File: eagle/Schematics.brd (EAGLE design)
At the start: 65 x 56 mm, 56 parts, among them K1 PIN20X2

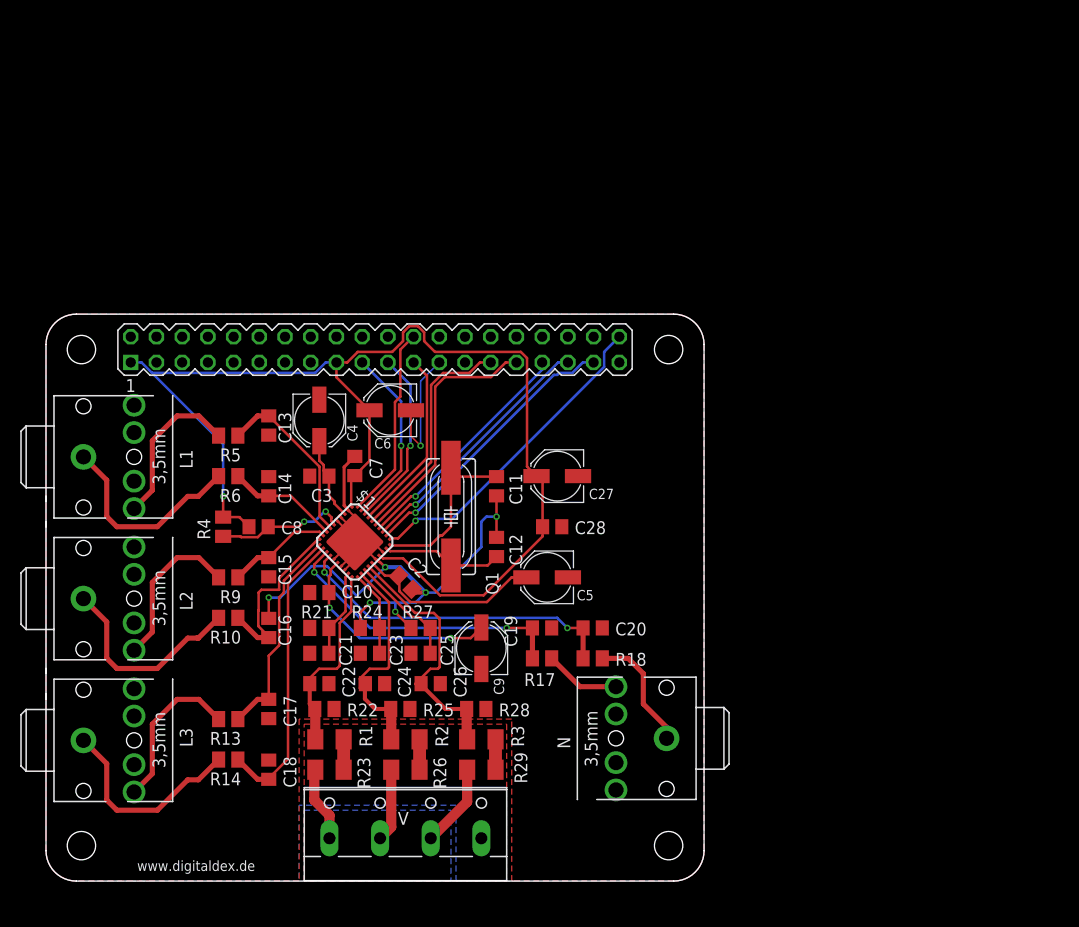
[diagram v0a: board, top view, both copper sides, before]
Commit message: fixed symbol; routed GND; rerouted some signals with more space
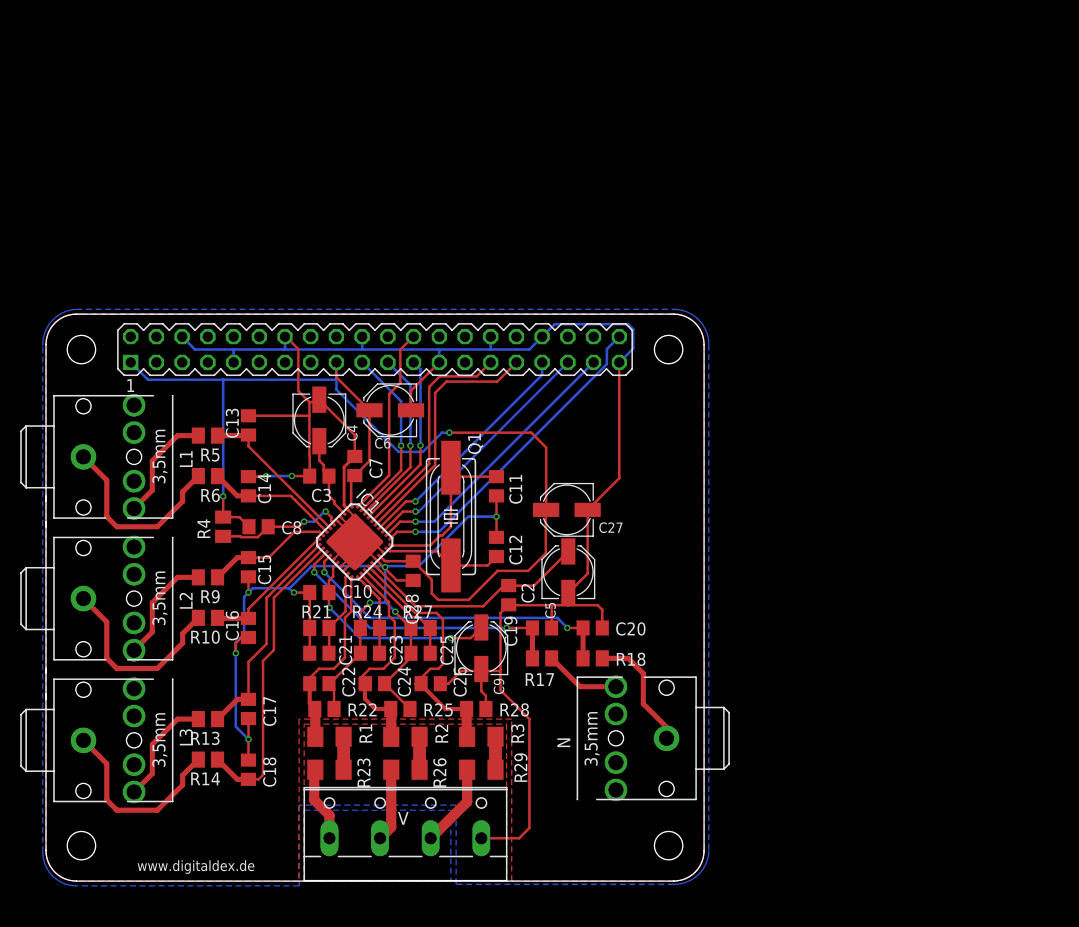
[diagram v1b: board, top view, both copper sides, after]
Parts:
- moved C28 14.4 mm to (36.3, 30.6), turned to 270 degrees
- moved C2 10.3 mm to (45.7, 28.2), turned to 270 degrees
- moved C27 3.47 mm to (51.5, 36.7)
- moved C5 2.15 mm to (51.6, 30.5), turned to 90 degrees
- moved C14 2.00 mm to (20.0, 39.0)
- moved C15 2.00 mm to (20.0, 31.0)
- moved C16 2.00 mm to (20.0, 25.0), turned to 270 degrees
- moved C17 2.00 mm to (20.0, 17.0)
- moved C18 2.00 mm to (20.0, 11.0)
- moved R10 2.00 mm to (16.0, 26.0)
- moved R13 2.00 mm to (16.0, 16.0)
- moved R14 2.00 mm to (16.0, 12.0)
- moved R5 2.00 mm to (16.0, 44.0)
- moved R6 2.00 mm to (16.0, 40.0)
- moved R9 2.00 mm to (16.0, 30.0)
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- renumbered $1 to IC1
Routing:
- net GND: track 96.0 -> 307.2 mm, vias 7 -> 10
- net N$10: track 15.8 -> 11.0 mm
- net N$14: track 15.8 -> 11.0 mm
- net N$12: track 15.8 -> 11.0 mm
- net N$4: track 18.6 -> 23.3 mm
- net +3V3: track 118.5 -> 114.2 mm, vias 1 -> 2
- net IBN: track 17.6 -> 13.9 mm
- net IBP: track 10.4 -> 12.4 mm
- net IAN: track 11.0 -> 13.0 mm
- net IAP: track 17.4 -> 15.5 mm
- net N$13: track 20.5 -> 18.9 mm
- net N$15: track 20.4 -> 18.9 mm
- net N$11: track 20.4 -> 18.9 mm
- net ICN: track 29.2 -> 30.2 mm
- net N$3: track 23.2 -> 24.2 mm
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
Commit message: Changes
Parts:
- removed C14, C15, C16, C17, C18, C19, C20, C21, C22, C23, C24, C25, C26: 22nF, resistor:C0805
- removed C27: 10uF, resistor:PANASONIC_C
- removed C28: 0.1uF, resistor:C0805
- removed IC1: ADE9000, ADE9000:LFCSP40
- removed K1: PIN20X2, FLYFISH:PIN_20X2
- removed R10, R13, R14, R17, R18, R21, R22, R24, R25, R27, R28, R5, R6, R9: 1k, resistor:M0805
- removed R23, R26, R29: 500k, resistor:M1206
- removed R4: 10k, resistor:M0805
- removed V: (no value), con-wago-500:W237-4
- added ADE9000: ADE9000, ADE9000:LFCSP40
- added ADUM4151: ADUM4151, ADUM4151:SOIC20R
- added ADUM6404: ADUM6404, ADUM6404:SOIC16R
- added C1: 1uF, resistor:C0805
- added C100, C110, C120, C200, C201, C202, C500, C501, C510, C511, C520, C521, C530, C531: 22nF, resistor:C0805
- added C101, C111, C121: 51pF, resistor:C0805
- added C30, C32, C40, C42, C50, C52: 0.1uF, resistor:C0805
- added C31, C33, C41, C43, C51, C53: 10uF, resistor:C0805
- added IRM05-5: (no value), meanwell_irm_v6:IRM_05/10
- added JP1: (no value), adafruit:2X20
- added L: (no value), con-wago-500:W237-4
- added R100, R101, R102, R103, R110, R111, R112, R113, R120, R121, R122, R123: 200k, resistor:M1206
- added R104, R114, R124, R200, R201, R202, R500, R501, R510, R511, R520, R521, R530, R531: 1k, resistor:M0805
- added U$1, U$2, U$3, U$4: (no value), holes:2,8
- added U$5: ADP122AUJZ-3.3-R7, ADP122AUJZ-3.3-R7:TSOT23-5L
- C11: value 20pF -> 10uF
- C12: value 20pF -> 0.1uF
- C13: value 22nF -> 4.7uF
- C2: value 0.22uF -> 0.1uF
- C3: value 0.22uF -> 4.7uF
- C4: value 4.7uF -> 0.1uF; device resistor:PANASONIC_C -> resistor:C0805
- C5: device resistor:PANASONIC_C -> resistor:C0805
- C6: value 10uF -> 0.1uF; device resistor:PANASONIC_C -> resistor:C0805
- C7: value 0.1uF -> 4.7uF
- C8: value 1uF -> 18pF
- C9: value 4.7uF -> 18pF; device resistor:PANASONIC_C -> resistor:C0805
- Q1: device crystal:HC49UP -> crystal:CTS406
- R1, R2, R3: value 500k -> 10k; device resistor:M1206 -> resistor:M0805
- moved L3 66.3 mm to (66.0, 1.00), turned to 90 degrees
- moved L2 54.2 mm to (48.0, 1.00), turned to 90 degrees
- moved L1 50.2 mm to (30.0, 1.00), turned to 90 degrees
- moved C11 29.1 mm to (19.0, 53.0), turned to 0 degrees
- moved C10 27.7 mm to (14.0, 53.0)
- moved C4 27.7 mm to (53.0, 36.0), turned to 0 degrees
- moved C13 25.8 mm to (41.0, 30.0)
- moved N 23.9 mm to (84.0, 1.00), turned to 90 degrees
- moved R1 21.7 mm to (39.0, 33.0), turned to 270 degrees
- moved C7 21.7 mm to (52.0, 44.0)
- moved C8 20.9 mm to (41.0, 41.0), turned to 180 degrees
- moved R2 20.1 mm to (48.0, 30.0), turned to 90 degrees
- moved C9 20.1 mm to (45.0, 43.0)
- moved C3 18.9 mm to (43.0, 30.0), turned to 270 degrees
- moved R3 18.1 mm to (52.0, 30.0), turned to 270 degrees
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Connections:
- removed net +3V3: C27.+, C28.1, C6.+, C7.1, C8.1, IC1.1, IC1.27, K1.1, K1.17, R4.2
- removed net N$2: IC1.33, K1.35
- removed net N$24: IC1.39, K1.19
- removed net N$25: IC1.38, K1.21
- removed net N$26: IC1.37, K1.23
- removed net N$27: IC1.40, K1.24
- removed net N$5: C3.1, C4.+, IC1.3
- removed net N$6: C8.2, IC1.6, R4.1
- removed net N$7: C10.1, C9.+, IC1.16
- removed net N$8: C11.1, IC1.30, Q1.2
- removed net N$9: C12.2, IC1.29, Q1.1
- new net +3V3_ADE: ADE9000.1, ADE9000.27, ADE9000.4, ADUM4151.20, C12.1, C13.1, C32.1, C33.1, C52.1, C53.1, R1.2, R3.2, U$5.5
- new net +3V3_ISO: ADUM4151.1, C30.1, C31.1, JP1.1, JP1.17
- new net +5V_ADE: ADUM6404.10, ADUM6404.16, C42.1, C43.1, C50.1, C51.1, U$5.1, U$5.3
- new net +5V_ISO: ADUM6404.1, ADUM6404.7, C10.1, C11.1, C40.1, C41.1, IRM05-5.V+, JP1.2, JP1.4
- new net AGND: ADUM4151.10, ADUM4151.2, ADUM4151.9, ADUM6404.2, ADUM6404.8, C10.2, C11.2, C30.2, C31.2, C40.2, C41.2, IRM05-5.V-, JP1.14, JP1.20, JP1.25, JP1.30, JP1.34, JP1.39, JP1.6, JP1.9
- new net AVDDOUT: ADE9000.25, C6.1, C7.1
- new net CF1_ADE: ADE9000.33, ADUM6404.12
- new net CF1_ISO: ADUM6404.5, JP1.31
- new net CF2_ADE: ADE9000.34, ADUM6404.11
- new net CF2_ISO: ADUM6404.6, JP1.33
- new net CLKIN: ADE9000.29, C9.1, Q1.3
- new net CLKOUT: ADE9000.30, C8.1, Q1.1
- new net DVDDOUT: ADE9000.3, C2.1, C3.1
- new net IRQ0_ADE: ADE9000.31, ADUM6404.14
- new net IRQ0_ISO: ADUM6404.3, JP1.27
- new net IRQ1_ADE: ADE9000.32, ADUM6404.13
- new net IRQ1_ISO: ADUM6404.4, JP1.29
- new net MISO_ADE: ADE9000.38, ADUM4151.16
- new net MISO_ISO: ADUM4151.5, JP1.21
- new net MOSI_ADE: ADE9000.39, ADUM4151.17
- new net MOSI_ISO: ADUM4151.4, JP1.19
- new net PM1_ADE: ADE9000.5, ADUM4151.14, R2.2
- new net PM1_ISO: ADUM4151.7, JP1.35
- new net REF: ADE9000.16, C4.1, C5.1
- new net RESET_ADE: ADE9000.6, ADUM4151.13, C1.1, R3.1
- new net RESET_ISO: ADUM4151.8, JP1.37
- new net SCLK_ADE: ADE9000.37, ADUM4151.18
- new net SCLK_ISO: ADUM4151.3, JP1.23
- new net SS_ADE: ADE9000.40, ADUM4151.15, R1.1
- new net SS_ISO: ADUM4151.6, JP1.24
- net GND: now also ADE9000.15, ADE9000.17, ADE9000.18, ADE9000.2, ADE9000.26, ADE9000.28, ADE9000.35, ADE9000.36, ADE9000.GND, ADUM4151.11, ADUM4151.12, ADUM4151.19, ADUM6404.15, ADUM6404.9, C1.2, C100.1, C110.1, C12.2, C120.1, C13.2, C200.1, C201.1, C202.1, C32.2, C33.2, C4.2, C42.2, C43.2, C5.2, C50.2, C500.1, C501.2, C51.2, C510.1, C511.2, C52.2, C520.1, C521.2, C53.2, C530.1, C531.2, C6.2, C8.2, C9.2, IRM05-5.AC/N, L.4, R104.2, R114.2, R124.2, R2.1, R200.2, R201.2, R202.2, U$5.2, U$5.4; no longer C10.2, C11.2, C12.1, C13.1, C14.2, C15.1, C16.2, C17.1, C18.2, C19.1, C20.2, C21.1, C22.1, C23.1, C24.1, C25.1, C26.1, C27.-, C28.2, C4.-, C5.-, C6.-, C9.-, IC1.15, IC1.17, IC1.18, IC1.2, IC1.26, IC1.28, IC1.4, IC1.5, IC1.GND, K1.14, K1.20, K1.25, K1.30, K1.34, K1.39, K1.6, K1.9, R21.2, R22.2, R24.2, R25.2, R27.2, R28.2, V.4
- net IAN: now also ADE9000.8, C501.1, R501.1; no longer C14.1, IC1.8, R6.1
- net IAP: now also ADE9000.7, C500.2, R500.1; no longer C13.2, IC1.7, R5.1
- net IBN: now also ADE9000.10, C511.1, R511.1; no longer C16.1, IC1.10, R10.1
- net IBP: now also ADE9000.9, C510.2, R510.1; no longer C15.2, IC1.9, R9.1
- net ICN: now also ADE9000.12, C521.1, R521.1; no longer C18.1, IC1.12, R14.1
- net ICP: now also ADE9000.11, C520.2, R520.1; no longer C17.2, IC1.11, R13.1
- net INN: now also ADE9000.14, C531.1, R531.1; no longer C20.1, IC1.14, R18.1
- net INP: now also ADE9000.13, C530.2, R530.1; no longer C19.2, IC1.13, R17.1
- net N$1: now also R121.2, R122.1; no longer IC1.32, K1.37
- net N$10: now also R500.2; no longer R5.2
- net N$11: now also R501.2; no longer R6.2
- net N$12: now also R510.2; no longer R9.2
- net N$13: now also R511.2; no longer R10.2
- net N$14: now also R520.2; no longer R13.2
- net N$15: now also R521.2; no longer R14.2
- net N$16: now also R530.2; no longer R17.2
- net N$17: now also R531.2; no longer R18.2
- net N$18: now also R101.2, R102.1; no longer R23.2, V.1
- net N$19: now also R111.2, R112.1; no longer R26.2, V.2
- net N$20: now also R112.2, R113.1; no longer R29.2, V.3
- net N$21: now also R122.2, R123.1; no longer IC1.35, K1.31
- net N$22: now also L.2, R113.2; no longer IC1.36, K1.29
- net N$23: now also IRM05-5.AC/L, L.3, R123.2; no longer IC1.31, K1.40
- net N$29: now also R110.2, R111.1; no longer R2.2, R26.1
- net N$3: now also R102.2, R103.1; no longer IC1.34, K1.33
- net N$30: now also R100.2, R101.1; no longer R1.2, R23.1
- net N$31: now also R120.2, R121.1; no longer R29.1, R3.2
- net N$4: now also L.1, R103.2; no longer C2.1, C5.+, IC1.25
- net VAN: now also ADE9000.19, C101.1, C200.2, R200.1; no longer C21.2, IC1.19, R21.1
- net VAP: now also ADE9000.20, C100.2, C101.2, R100.1, R104.1; no longer C22.2, IC1.20, R1.1, R22.1
- net VBN: now also ADE9000.21, C111.1, C201.2, R201.1; no longer C23.2, IC1.21, R24.1
- net VBP: now also ADE9000.22, C110.2, C111.2, R110.1, R114.1; no longer C24.2, IC1.22, R2.1, R25.1
- net VCN: now also ADE9000.23, C121.1, C202.2, R202.1; no longer C25.2, IC1.23, R27.1
- net VCP: now also ADE9000.24, C120.2, C121.2, R120.1, R124.1; no longer C26.2, IC1.24, R28.1, R3.1
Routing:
- net GND: track 307.2 -> 181.7 mm, vias 10 -> 11
- net +3V3: track 114.2 -> 0.00 mm, vias 2 -> 0
- net +3V3_ADE: track 0.00 -> 100.5 mm, vias 0 -> 4
- net +5V_ISO: track 0.00 -> 80.2 mm, vias 0 -> 2
- net RESET_ISO: track 0.00 -> 53.7 mm
- net +3V3_ISO: track 0.00 -> 50.3 mm, vias 0 -> 2
- net PM1_ISO: track 0.00 -> 49.5 mm
- net VAN: track 9.56 -> 53.1 mm
- net VAP: track 19.4 -> 52.9 mm
- net RESET_ADE: track 0.00 -> 32.3 mm
- net CF2_ISO: track 0.00 -> 31.2 mm
- net VBN: track 8.33 -> 38.2 mm
- net SS_ISO: track 0.00 -> 29.3 mm
- net IAP: track 15.5 -> 44.0 mm
- net +5V_ADE: track 0.00 -> 28.1 mm
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- added copper zone on layer 1, net AGND
- added copper zone on layer 16, net AGND
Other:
- board size 65 x 56 mm -> 99.7 x 80.2 mm
- board text added: "ADP122"
- board text added: "ADUM6404"
- board text added: "L1"
- board text added: "L2"
- board text added: "L3"
- board text added: "N"

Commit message: Changes
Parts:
- removed L: (no value), con-wago-500:W237-4
- added R502, R503, R512, R513, R522, R523, R532, R533: 5.1, Schematics:M0805
- added X1: MSTBA4, Schematics:MSTBA4
- ADE9000: device ADE9000:LFCSP40 -> Schematics:LFCSP40
- ADUM4151: device ADUM4151:SOIC20R -> Schematics:SOIC20R
- ADUM6404: device ADUM6404:SOIC16R -> Schematics:SOIC16R
- C1, C10, C100, C101, C11, C110, C111, C12, C120, C121, C13, C2, C200, C201, C202, C3, C30, C31, C32, C33, C4, C40, C41, C42, C43, C5, C50, C500, C501, C51, C510, C511, C52, C520, C521, C53, C530, C531, C6, C7, C8, C9: device resistor:C0805 -> Schematics:C0805
- IRM05-5: device meanwell_irm_v6:IRM_05/10 -> Schematics:IRM_05/10
- JP1: device adafruit:2X20 -> Schematics:2X20
- L1, L2, L3, N: device adafruit:STX3100 -> Schematics:STX3100
- Q1: device crystal:CTS406 -> Schematics:CTS406
- R1, R104, R114, R124, R2, R200, R201, R202, R3, R500, R501, R510, R511, R520, R521, R530, R531: device resistor:M0805 -> Schematics:M0805
- R100, R101, R102, R103, R110, R111, R112, R113, R120, R121, R122, R123: device resistor:M1206 -> Schematics:M1206
- U$5: device ADP122AUJZ-3.3-R7:TSOT23-5L -> Schematics:TSOT23-5L
- moved U$2 116.8 mm to (4.00, 4.00)
- moved U$4 116.8 mm to (96.0, 76.0)
- moved JP1 5.10 mm to (4.00, 40.0)
- moved R500 2.00 mm to (27.0, 17.0)
- moved R501 2.00 mm to (33.0, 17.0)
- moved R510 2.00 mm to (45.0, 17.0)
- moved R511 2.00 mm to (51.0, 17.0)
- moved R520 2.00 mm to (63.0, 17.0)
- moved R521 2.00 mm to (69.0, 17.0)
- moved R530 2.00 mm to (81.0, 17.0)
- moved R531 2.00 mm to (87.0, 17.0)
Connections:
- net GND: now also R502.2, R503.1, R512.2, R513.1, R522.2, R523.1, R532.2, R533.1, X1.4; no longer L.4
- net N$10: now also R502.1
- net N$11: now also R503.2
- net N$12: now also R512.1
- net N$13: now also R513.2
- net N$14: now also R522.1
- net N$15: now also R523.2
- net N$16: now also R532.1
- net N$17: now also R533.2
- net N$22: now also X1.2; no longer L.2
- net N$23: now also X1.3; no longer L.3
- net N$4: now also X1.1; no longer L.1
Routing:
- net +5V_ISO: track 80.2 -> 89.2 mm
- net GND: track 181.7 -> 189.3 mm, vias 11 -> 15
- net CF2_ISO: track 31.2 -> 23.6 mm, vias 0 -> 1
- net RESET_ISO: track 53.7 -> 48.0 mm
- net PM1_ISO: track 49.5 -> 44.3 mm
- net SCLK_ISO: track 25.2 -> 20.2 mm
- net +3V3_ISO: track 50.3 -> 55.3 mm
- net MISO_ISO: track 25.7 -> 20.9 mm
- net SS_ISO: track 29.3 -> 24.6 mm
- net AGND: track 21.5 -> 26.0 mm
- net CF1_ISO: track 24.5 -> 20.7 mm, vias 0 -> 1
- net MOSI_ISO: track 22.1 -> 25.0 mm
- net ICP: track 27.8 -> 25.8 mm
- net ICN: track 30.0 -> 28.0 mm
- net IBN: track 25.3 -> 23.3 mm
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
